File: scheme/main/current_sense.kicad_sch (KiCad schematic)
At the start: 4 parts, among them U2 ACS712xLCTR-05B

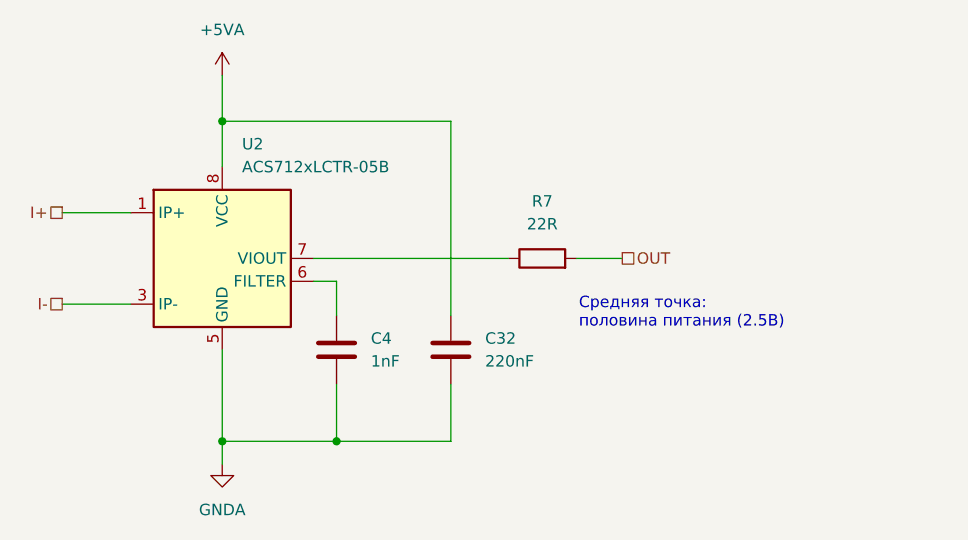
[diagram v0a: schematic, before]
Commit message: bootstrap dc-dc add capacitors & more
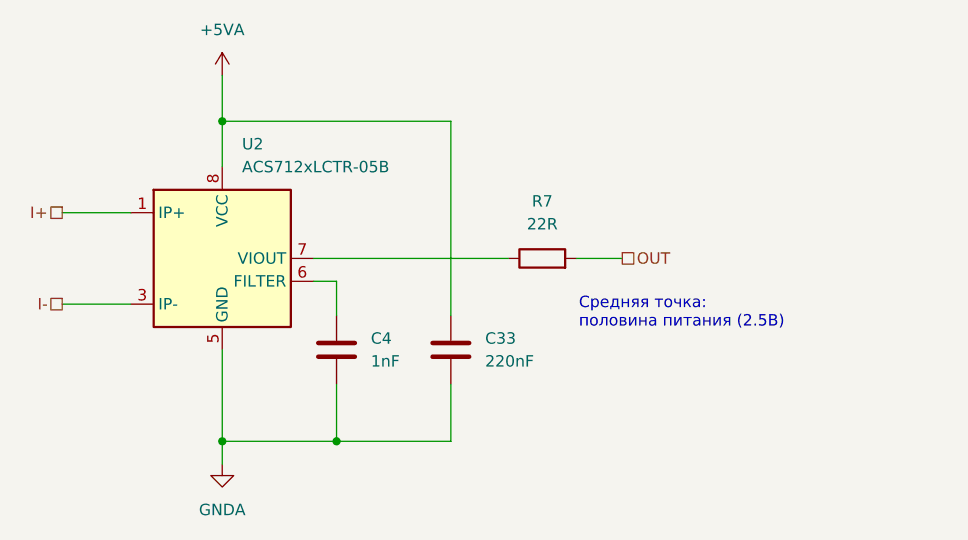
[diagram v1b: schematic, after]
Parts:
- renumbered C32 to C33
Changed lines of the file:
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@@
 		(dnp no)
 		(fields_autoplaced yes)
-		(property "Reference" "C32"
+		(property "Reference" "C33"
 			(at 135.89 100.3299 0)
 			(effects

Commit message: control isolation schematic
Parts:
- R7: footprint (none) -> Resistor_SMD:R_0805_2012Metric
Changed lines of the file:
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@@
 			)
 		)
-		(property "Footprint" ""
+		(property "Footprint" "Resistor_SMD:R_0805_2012Metric"
 			(at 142.24 93.218 90)
 			(effects
